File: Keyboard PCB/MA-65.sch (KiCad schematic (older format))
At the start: 151 parts, among them J1 USB_B_Mini, SW1 SW_Push, SW12 ESC, SW13 Tab, SW14 L Shift, SW15 L Ctrl, SW16 1, SW17 Q, SW18 A, SW19 S, SW2 `, SW20 2, SW21 W, SW22 Z, SW23 L Alt, SW24 3, SW25 E, SW26 D, SW27 X, SW28 4, SW29 R, SW3 PgUp, SW30 F, SW31 C, SW32 5, SW33 T, SW34 G, SW35 V, SW36 6, SW37 Y, SW38 H, SW39 B, SW4 PgDown, SW40 Space, SW41 7, SW42 U, SW43 J, SW44 N, SW45 8, SW46 I, SW47 K, SW48 M, SW49 9, SW5 Fn, SW50 O, SW51 L, SW52 ,, SW53 AltGr, SW54 ;, SW56 0, SW57 P, SW58 ., SW59 R Ctrl, SW6 Right, SW60 -, SW61 [, SW62 ', SW63 /, SW64 =, SW65 ], SW66 RShift, SW67 Left, SW68 Back Space, SW69 \\, SW7 Back Space 2u, SW70 Enter, SW71 UP, SW72 Down, SW91 Caps, U1 ATmega32U4-AU, Y1 16mhz

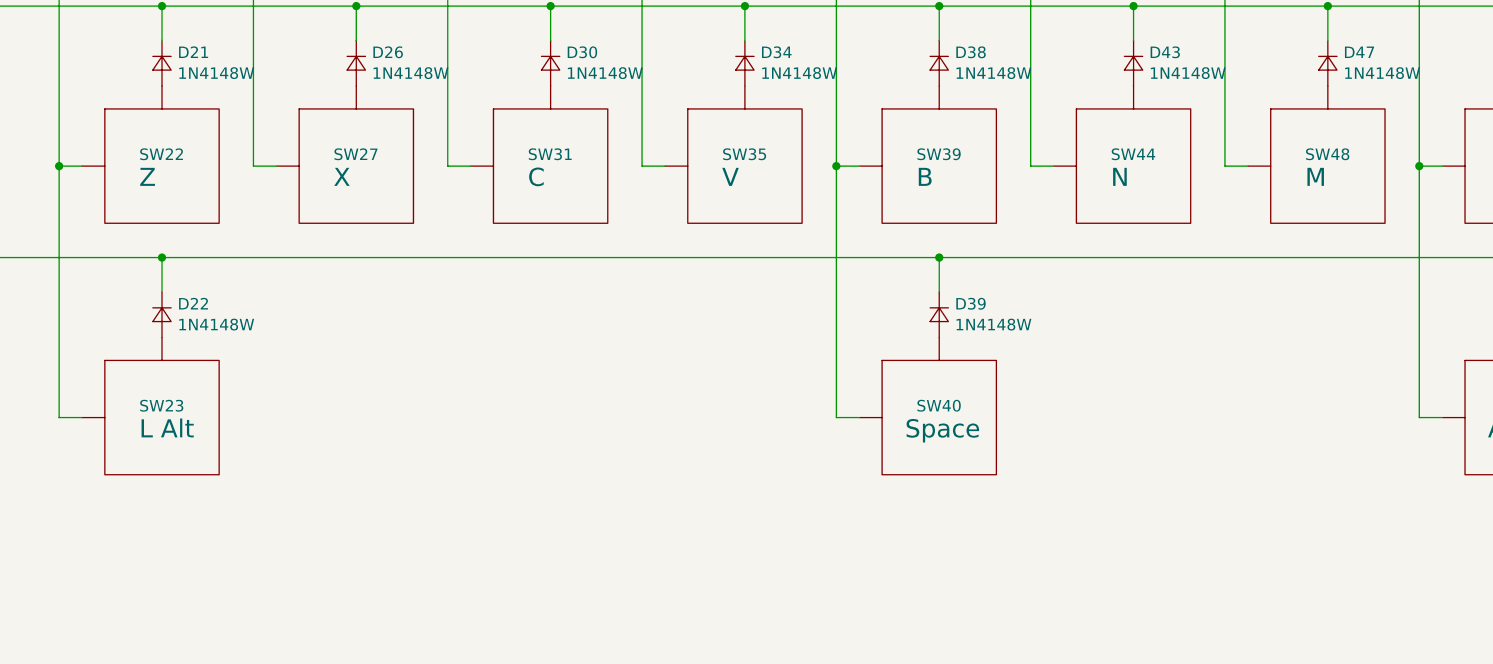
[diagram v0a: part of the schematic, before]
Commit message: Split spacebar Ma-65
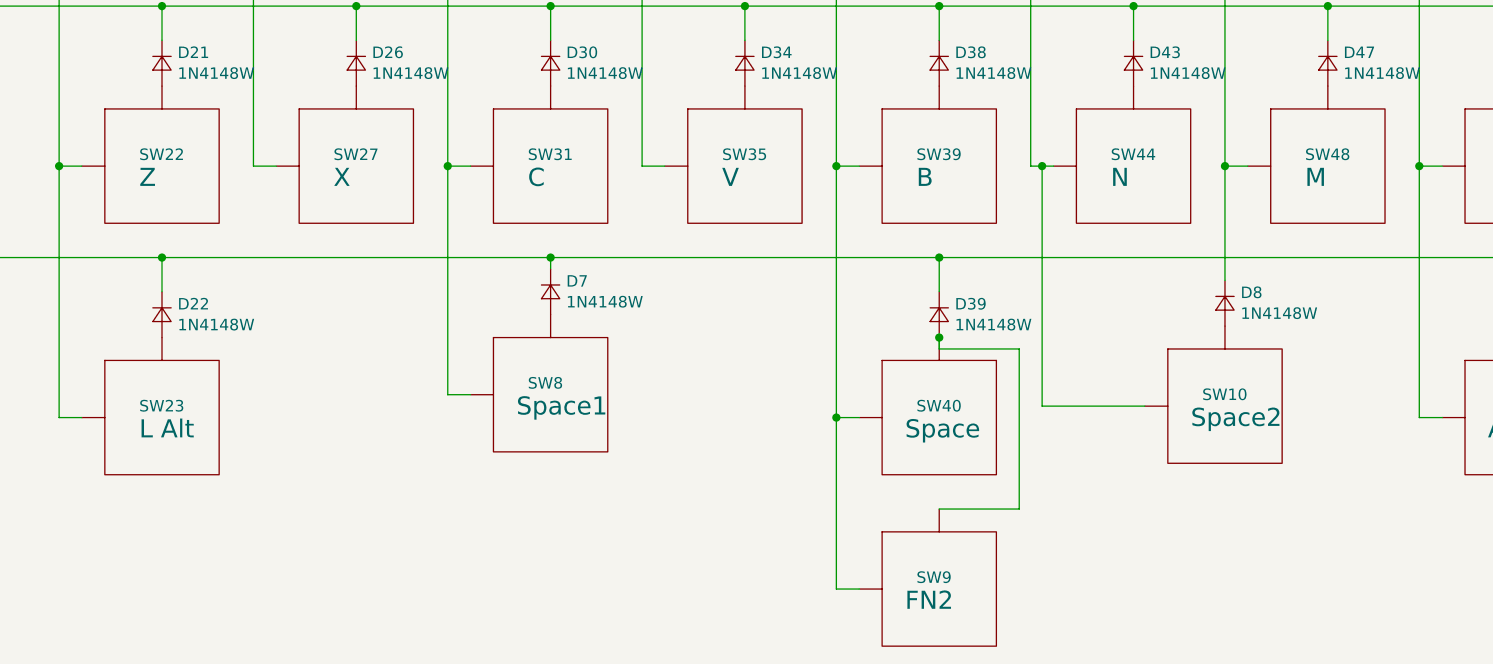
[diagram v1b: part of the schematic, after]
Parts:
- added D7, D8: 1N4148W, Diode_SMD:D_SOD-123, symbol Device:D_Small
- added SW10: Space2, acheron_MX:MX225, symbol acheronSymbols:MXSwitch
- added SW8: Space1, acheron_MX:MX275, symbol acheronSymbols:MXSwitch
- added SW9: FN2, acheron_MX:MX100, symbol acheronSymbols:MXSwitch
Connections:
- net COL7: now also SW9.1 (Col)
- net COL8: now also SW10.1 (Col)
- net COL9: now also D8.1 (K)
- net at D14.1 (K), D22.1 (K), D39.1 (K)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: now also D7.1 (K)
- net at SW28.1 (Col), SW29.1 (Col), SW30.1 (Col)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: now also SW8.1 (Col)
- net at D39.2 (A), SW40.2 (Row): now also SW9.2 (Row)
- new net: D7.2 (A), SW8.2 (Row)
- new net: D8.2 (A), SW10.2 (Row)
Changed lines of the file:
@@
 Connection ~ 9750 9600
 Wire Wire Line
-	10250 10300 10150 10300
+	10250 10300 10200 10300
 Wire Wire Line
 	11000 10300 11000 9200
@@
 Connection ~ 5900 10300
 Wire Wire Line
-	6350 10700 9750 10700
+	6350 10700 8050 10700
 Connection ~ 6350 10700
 Wire Wire Line
@@
 	15000 10700 16500 10700
 Connection ~ 15000 10700
+Wire Wire Line
+	7700 11300 7600 11300
+$Comp
+L Device:D_Small D7
+U 1 1 5DF562D7
+P 8050 10850
+F 0 "D7" V 8004 10918 50  0000 L CNN
+F 1 "1N4148W" V 8095 10918 50  0000 L CNN
+F 2 "Diode_SMD:D_SOD-123" V 8050 10850 50  0001 C CNN
+F 3 "~" V 8050 10850 50  0001 C CNN
+	1    8050 10850
+	0    1    1    0
+$EndComp
+$Comp
+L acheronSymbols:MXSwitch SW8
+U 1 1 5DF562DD
+P 8050 11300
+F 0 "SW8" H 7950 11350 50  0000 L CNN
+F 1 "Space1" H 7900 11250 79  0000 L CNN
+F 2 "acheron_MX:MX275" H 8050 11300 50  0001 C CNN
+F 3 "" H 8050 11300 50  0001 C CNN
+	1    8050 11300
+	1    0    0    -1
+$EndComp
+$Comp
+L Device:D_Small D8
+U 1 1 5DF877F1
+P 11000 10900
+F 0 "D8" V 10954 10968 50  0000 L CNN
+F 1 "1N4148W" V 11045 10968 50  0000 L CNN
+F 2 "Diode_SMD:D_SOD-123" V 11000 10900 50  0001 C CNN
+F 3 "~" V 11000 10900 50  0001 C CNN
+	1    11000 10900
+	0    1    1    0
+$EndComp
+$Comp
+L acheronSymbols:MXSwitch SW10
+U 1 1 5DF877F7
+P 11000 11350
+F 0 "SW10" H 10900 11400 50  0000 L CNN
+F 1 "Space2" H 10850 11300 79  0000 L CNN
+F 2 "acheron_MX:MX225" H 11000 11350 50  0001 C CNN
+F 3 "" H 11000 11350 50  0001 C CNN
+	1    11000 11350
+	1    0    0    -1
+$EndComp
+Connection ~ 7600 10300
+Wire Wire Line
+	10200 11350 10200 10300
+Wire Wire Line
+	10200 11350 10650 11350
+Connection ~ 10200 10300
+Wire Wire Line
+	10200 10300 10150 10300
+$Comp
+L acheronSymbols:MXSwitch SW9
+U 1 1 5DFEDA5D
+P 9750 12150
+F 0 "SW9" H 9650 12200 50  0000 L CNN
+F 1 "FN2" H 9600 12100 79  0000 L CNN
+F 2 "acheron_MX:MX100" H 9750 12150 50  0001 C CNN
+F 3 "" H 9750 12150 50  0001 C CNN
+	1    9750 12150
+	1    0    0    -1
+$EndComp
+Wire Wire Line
+	9400 12150 9300 12150
+Wire Wire Line
+	9300 12150 9300 11400
+Connection ~ 9300 11400
+Wire Wire Line
+	11000 10800 11000 10300
+Connection ~ 11000 10300
+Wire Wire Line
+	7600 10300 7600 11300
+Wire Wire Line
+	8050 10750 8050 10700
+Connection ~ 8050 10700
+Wire Wire Line
+	8050 10700 9750 10700
+Wire Wire Line
+	9750 11800 10100 11800
+Wire Wire Line
+	10100 11800 10100 11100
+Wire Wire Line
+	10100 11100 9750 11100
+Wire Wire Line
+	9750 11100 9750 11050
+Connection ~ 9750 11050
 $EndSCHEMATC

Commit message: PCB Ma-65
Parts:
- removed D7, D8: 1N4148W, Diode_SMD:D_SOD-123, symbol Device:D_Small
- removed SW10: Space2, acheron_MX:MX225, symbol acheronSymbols:MXSwitch
- removed SW8: Space1, acheron_MX:MX275, symbol acheronSymbols:MXSwitch
- removed SW9: FN2, acheron_MX:MX100, symbol acheronSymbols:MXSwitch
- added D10, D9: 1N4148W, Diode_SMD:D_SOD-123, symbol Device:D_Small
- added SW11: PgUp, acheron_MX:MX100, symbol acheronSymbols:MXSwitch
- added SW55: Win, acheron_MX:MX125, symbol acheronSymbols:MXSwitch
- SW2: value ` -> Del
- SW3: value PgUp -> PgDn
- SW4: value PgDown -> Insert
- SW5: value Fn -> Fn2
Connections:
- net COL13: no longer SW66.1 (Col), SW67.1 (Col)
- net COL14: now also SW66.1 (Col), SW67.1 (Col); no longer SW71.1 (Col), SW72.1 (Col)
- net COL15: now also SW71.1 (Col), SW72.1 (Col); no longer SW3.1 (Col), SW4.1 (Col), SW5.1 (Col), SW6.1 (Col)
- net COL2: now also SW55.1 (Col)
- net at D14.1 (K), D22.1 (K), D39.1 (K)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: now also D10.1 (K)
- net at D1.1 (K), D11.1 (K), D15.1 (K)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: now also D9.1 (K)
- new net: D9.2 (A), SW11.2 (Row)
- new net: D10.2 (A), SW55.2 (Row)
- new net COL16: SW11.1 (Col), SW3.1 (Col), SW4.1 (Col), SW5.1 (Col), SW6.1 (Col)
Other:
- moved on the sheet: D2, D3, D4, D5, D65, D66, D68, D69, D70, D71, SW3, SW4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
